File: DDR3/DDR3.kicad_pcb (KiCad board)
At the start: 2 copper layers, 67.6 x 30 mm, 1 part

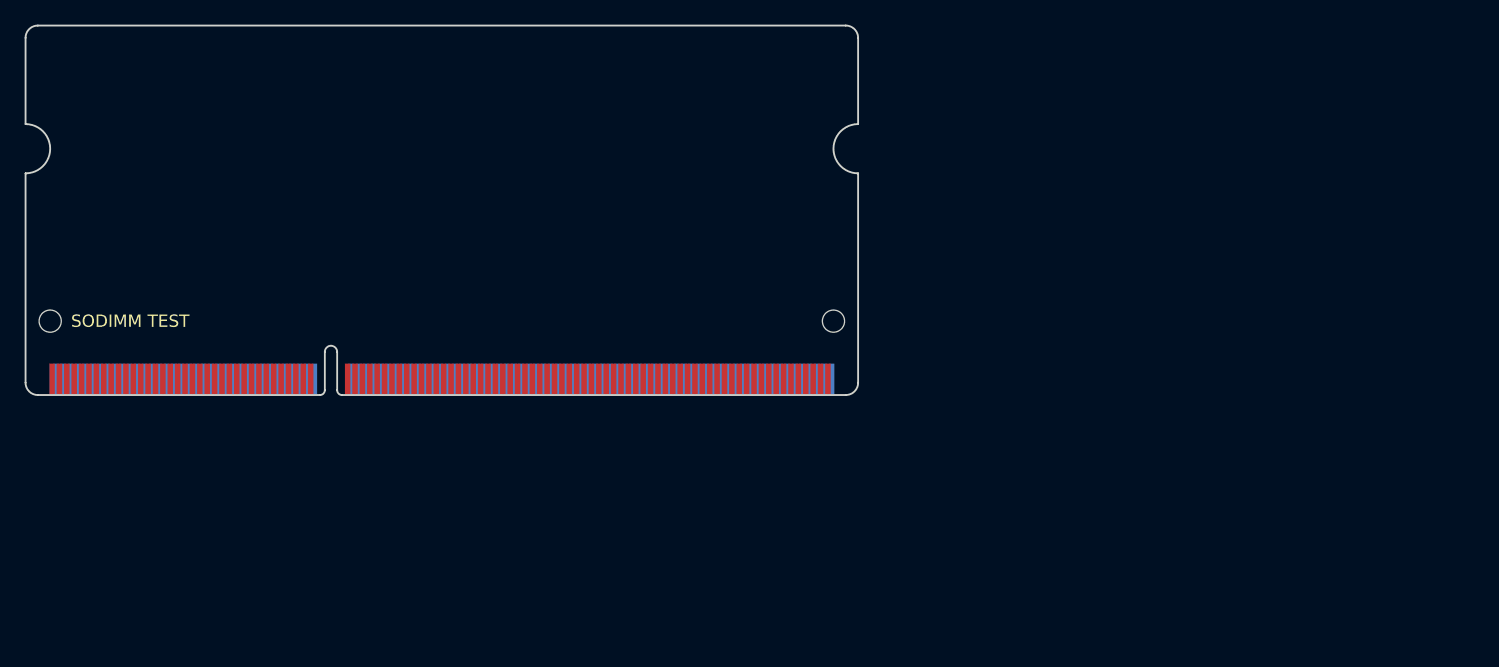
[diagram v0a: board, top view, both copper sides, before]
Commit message: ddr3: Move and follow spec better
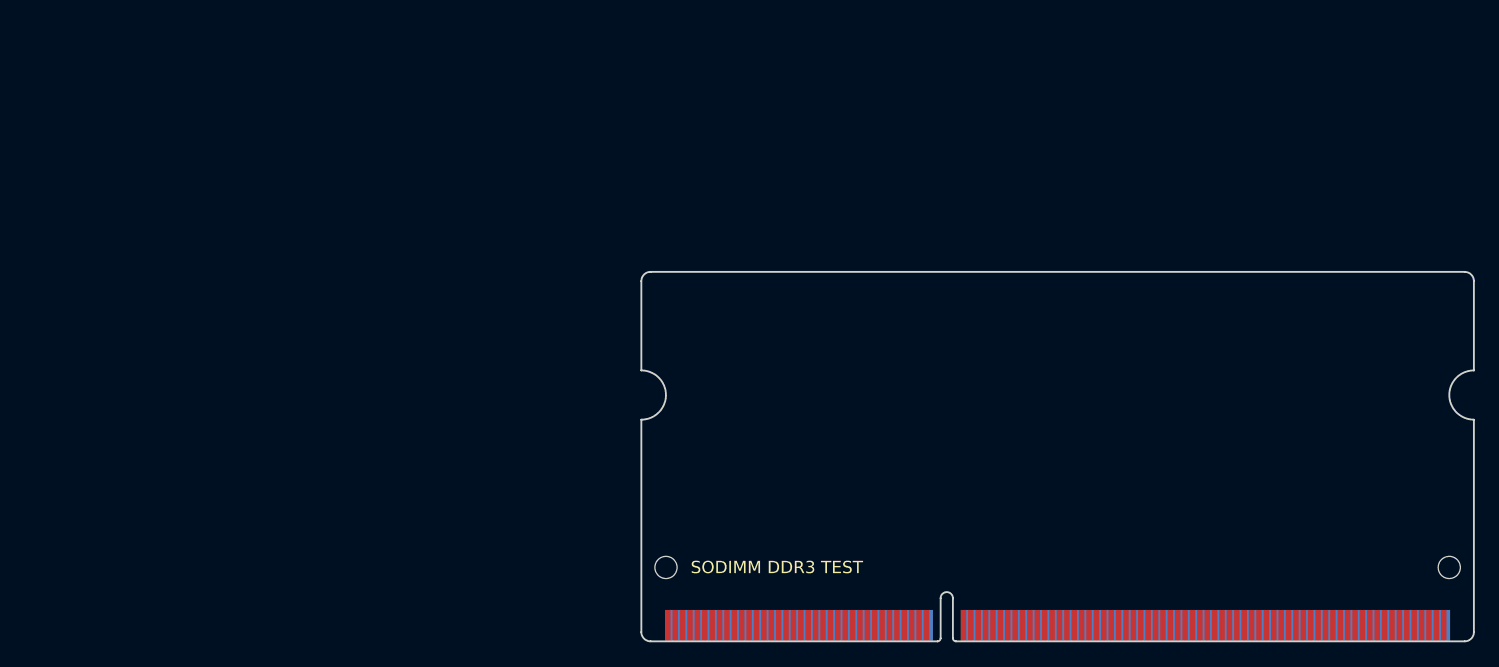
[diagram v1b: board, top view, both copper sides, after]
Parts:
- SODIMM DDR3 TEST: renamed from SODIMM TEST
- moved SODIMM DDR3 TEST 53.9 mm to (100.0, 100.0)
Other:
- outline, holes or cut-outs redrawn
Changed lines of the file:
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@@
   )
   (module SODIMM:SODIMM_DDR3_EDGE (layer F.Cu)
-    (at 50 80)
-    (fp_text reference "SODIMM TEST" (at 8.5 -6) (layer F.SilkS)
+    (at 100 100)
+    (fp_text reference "SODIMM DDR3 TEST" (at 11 -6) (layer F.SilkS)
       (effects (font (size 1 1) (thickness 0.15)))
     )
@@
     (pad "" np_thru_hole circle (at 65.6 -6) (size 1.8 1.8) (drill 1.8) (layers *.Cu *.Mask))
   )
-  (gr_arc (start 74.8 76.5) (end 74.3 76.5) (angle 180) (layer Edge.Cuts) (width 0.15))
-  (gr_arc (start 116.6 79) (end 117.6 79) (angle 90) (layer Edge.Cuts) (width 0.15))
-  (gr_arc (start 116.6 51) (end 116.6 50) (angle 90) (layer Edge.Cuts) (width 0.15))
-  (gr_arc (start 51 51) (end 50 51) (angle 90) (layer Edge.Cuts) (width 0.15))
-  (gr_arc (start 51 79) (end 51 80) (angle 90) (layer Edge.Cuts) (width 0.15))
-  (gr_arc (start 75.7 79.6) (end 75.7 80) (angle 90) (layer Edge.Cuts) (width 0.15))
-  (gr_arc (start 73.9 79.6) (end 74.3 79.6) (angle 90) (layer Edge.Cuts) (width 0.15))
-  (gr_line (start 51 80) (end 73.9 80) (layer Edge.Cuts) (width 0.15))
-  (gr_line (start 75.3 76.5) (end 75.3 79.6) (layer Edge.Cuts) (width 0.15))
-  (gr_line (start 74.3 76.5) (end 74.3 79.6) (layer Edge.Cuts) (width 0.15))
-  (gr_line (start 117.6 58) (end 117.6 51) (layer Edge.Cuts) (width 0.15))
-  (gr_arc (start 117.6 60) (end 117.6 62) (angle 180) (layer Edge.Cuts) (width 0.15))
-  (gr_line (start 50 51) (end 50 58) (layer Edge.Cuts) (width 0.15))
-  (gr_line (start 116.6 50) (end 51 50) (layer Edge.Cuts) (width 0.15))
-  (gr_arc (start 50 60) (end 50 58) (angle 180) (layer Edge.Cuts) (width 0.15))
-  (gr_line (start 117.6 62) (end 117.6 79) (layer Edge.Cuts) (width 0.15))
-  (gr_line (start 75.7 80) (end 116.6 80) (layer Edge.Cuts) (width 0.15))
-  (gr_line (start 50 62) (end 50 79) (layer Edge.Cuts) (width 0.15))
+  (gr_arc (start 124.8 96.5) (end 124.3 96.5) (angle 180) (layer Edge.Cuts) (width 0.15))
+  (gr_arc (start 166.85 99.25) (end 167.6 99.25) (angle 90) (layer Edge.Cuts) (width 0.15))
+  (gr_arc (start 166.85 70.75) (end 166.85 70) (angle 90) (layer Edge.Cuts) (width 0.15))
+  (gr_arc (start 100.75 70.75) (end 100 70.75) (angle 89.9) (layer Edge.Cuts) (width 0.15))
+  (gr_arc (start 100.75 99.25) (end 100.75 100) (angle 90) (layer Edge.Cuts) (width 0.15))
+  (gr_arc (start 125.55 99.75) (end 125.55 100) (angle 90) (layer Edge.Cuts) (width 0.15))
+  (gr_arc (start 124.05 99.75) (end 124.3 99.75) (angle 90) (layer Edge.Cuts) (width 0.15))
+  (gr_line (start 100.75 100) (end 124.05 100) (layer Edge.Cuts) (width 0.15))
+  (gr_line (start 125.3 96.5) (end 125.3 99.75) (layer Edge.Cuts) (width 0.15))
+  (gr_line (start 124.3 96.5) (end 124.3 99.75) (layer Edge.Cuts) (width 0.15))
+  (gr_line (start 167.6 78) (end 167.6 70.75) (layer Edge.Cuts) (width 0.15))
+  (gr_arc (start 167.6 80) (end 167.6 82) (angle 180) (layer Edge.Cuts) (width 0.15))
+  (gr_line (start 100 70.75) (end 100 78) (layer Edge.Cuts) (width 0.15))
+  (gr_line (start 166.85 70) (end 100.75 70) (layer Edge.Cuts) (width 0.15))
+  (gr_arc (start 100 80) (end 100 78) (angle 180) (layer Edge.Cuts) (width 0.15))
+  (gr_line (start 167.6 82) (end 167.6 99.25) (layer Edge.Cuts) (width 0.15))
+  (gr_line (start 125.55 100) (end 166.85 100) (layer Edge.Cuts) (width 0.15))
+  (gr_line (start 100 82) (end 100 99.25) (layer Edge.Cuts) (width 0.15))
   (zone (net 0) (net_name "") (layer F.Mask) (hatch edge 0.508)
     (connect_pads (clearance 0.508))
@@
     (polygon
       (pts
-        (xy 73 77.25) (xy 76 77.25) (xy 76 80.15) (xy 73 80.15)
+        (xy 123 97.25) (xy 126 97.25) (xy 126 100.15) (xy 123 100.15)
       )
     )
@@
     (polygon
       (pts
-        (xy 73.5 77.25) (xy 76.5 77.25) (xy 76.5 80.15) (xy 73.5 80.15)
+        (xy 123.5 97.25) (xy 126.5 97.25) (xy 126.5 100.15) (xy 123.5 100.15)
       )
     )
